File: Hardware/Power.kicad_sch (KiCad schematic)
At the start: 26 parts, among them U2 LT1963AEST-3.3#TRPBF, U3 LT1963AEST-3.3#TRPBF

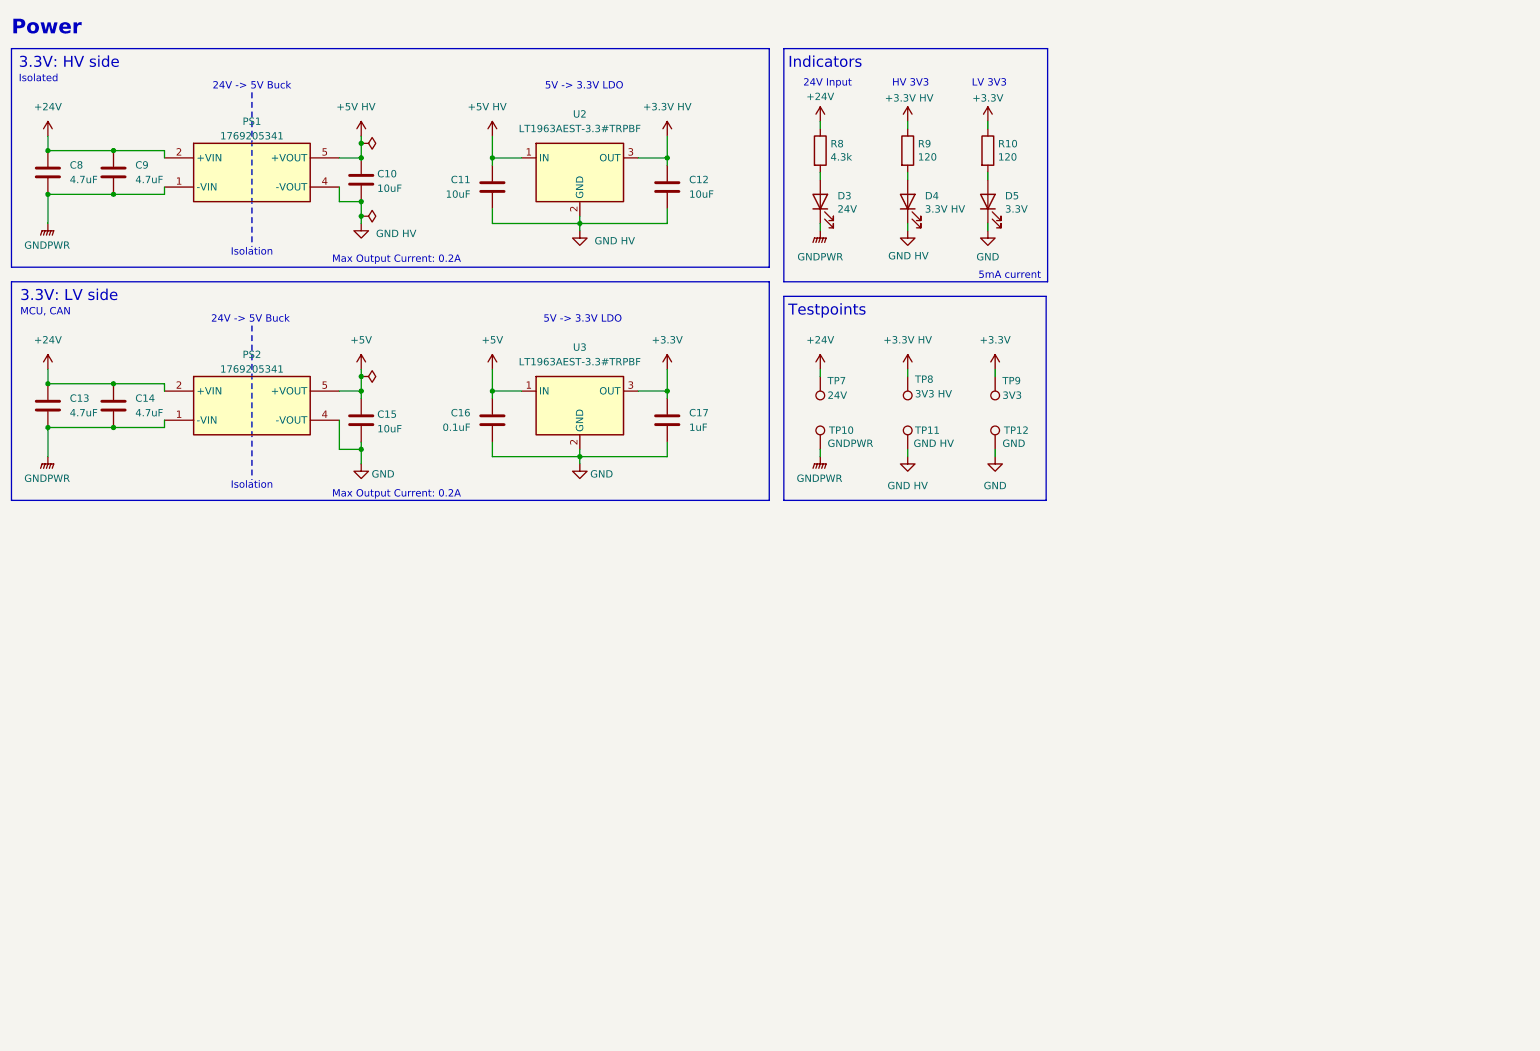
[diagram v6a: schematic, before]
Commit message: 24-5 buck from psom, OR gate for bootload. more sheet organization
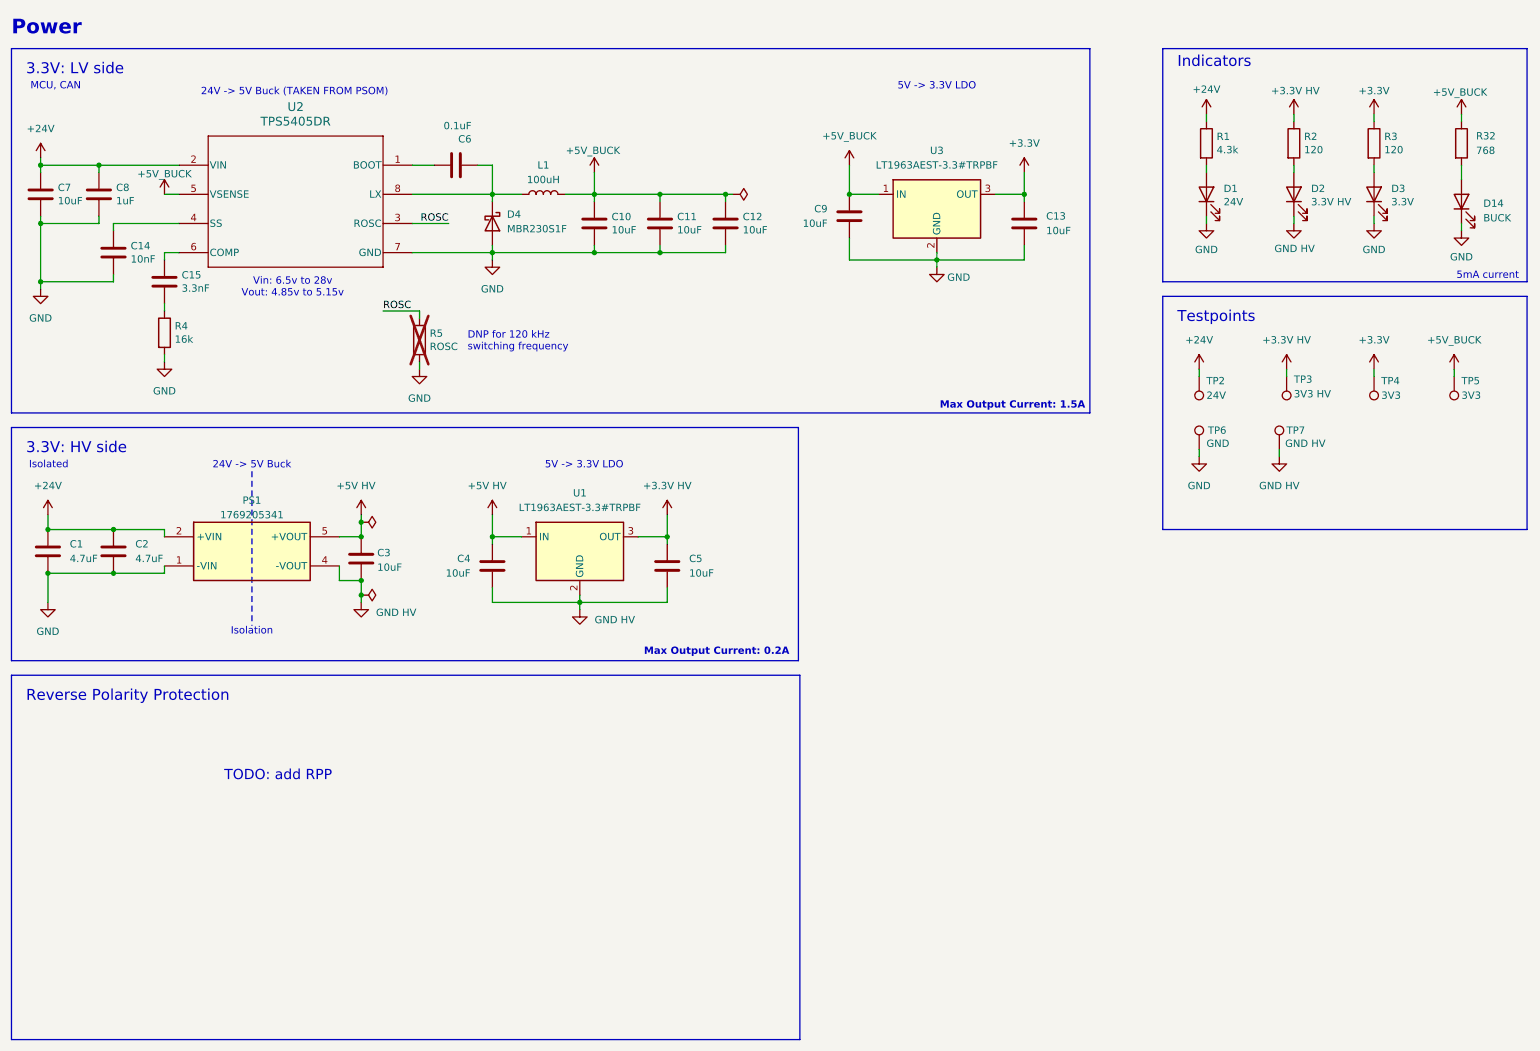
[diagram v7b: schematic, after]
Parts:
- removed C13: 4.7uF, Capacitor_SMD:C_0603_1608Metric_Pad1.08x0.95mm_HandSolder, symbol Device:C
- removed PS2: 1769205341, Parts:WE_1769205341, symbol WE_1769205341:1769205341
- removed TP10: GNDPWR, symbol Connector:TestPoint
- added C10, C11, C12, C7: 10uF, Capacitor_SMD:C_0805_2012Metric_Pad1.18x1.45mm_HandSolder, symbol Device:C
- added C6: 0.1uF, Capacitor_SMD:C_0603_1608Metric_Pad1.08x0.95mm_HandSolder, symbol Device:C
- added C8: 1uF, Capacitor_SMD:C_0603_1608Metric_Pad1.08x0.95mm_HandSolder, symbol Device:C
- added D14: BUCK, LED_SMD:LED_0603_1608Metric_Pad1.05x0.95mm_HandSolder, symbol Device:LED
- added D4: MBR230S1F, Diode_SMD:D_SOD-123F, symbol Device:D_Schottky
- added L1: 100uH, Inductor_SMD:L_Coilcraft_MSS1246-XXX, symbol Device:L
- added R32: 768, Resistor_SMD:R_0603_1608Metric_Pad0.98x0.95mm_HandSolder, symbol Device:R
- added R4: 16k, Resistor_SMD:R_0603_1608Metric_Pad0.98x0.95mm_HandSolder, symbol Device:R
- added R5: ROSC, Resistor_SMD:R_0603_1608Metric_Pad0.98x0.95mm_HandSolder, symbol Device:R
- added TP5: 3V3, symbol Connector:TestPoint
- added U2: TPS5405DR, UTSVT_Power:TPS5405DR, symbol utsvt-power:TPS5405DR
- C13: renamed from C17; value 1uF -> 10uF
- C14: value 4.7uF -> 10nF; P/N (none) -> MSASH168SB5103KTNA01
- C15: value 10uF -> 3.3nF; P/N (none) -> 06035C332K4T2A
- C9: renamed from C16; value 0.1uF -> 10uF
- renumbered C8 to C1, C9 to C2, C10 to C3, C11 to C4, C12 to C5, D3 to D1, D4 to D2, D5 to D3, R8 to R1, R9 to R2, R10 to R3, TP7 to TP2, TP8 to TP3, TP9 to TP4, TP12 to TP6, TP11 to TP7, U2 to U1
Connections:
- net GNDPWR is gone; now on net GND: C1.2, C14.2, C2.2, D1.1 (K), PS1.1 (-VIN)
- net +24V: now also C7.1, C8.1, U2.2 (VIN); no longer C14.1
- net GND: now also C10.2, C11.2, C12.2, C7.2, C8.2, D14.1 (K), D4.2 (A), R4.2, R5.2, U2.7 (GND); no longer C15.2
- net +5V renamed +5V_BUCK
- net +5V_BUCK: now also C10.1, C11.1, C12.1, L1.2, R32.1, TP5.1, U2.5 (VSENSE); no longer C15.1
- new net: C6.2, D4.1 (K), L1.1, U2.8 (LX)
- new net: D14.2 (A), R32.2
- new net: C6.1, U2.1 (BOOT)
- new net: C14.1, U2.4 (SS)
- new net: C15.1, U2.6 (COMP)
- new net: C15.2, R4.1
- new net ROSC: R5.1, U2.3 (ROSC)
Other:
- note added: "24V -> 5V Buck (TAKEN FROM PSOM)"
- note added: "DNP for 120 kHz switching frequency"
- note added: "Max Output Current: 1.5A"
- note added: "Reverse Polarity Protection"
- note added: "TODO: add RPP"
- note added: "Vin: 6.5v to 28v Vout: 4.85v to 5.15v"
- note removed: "24V Input"
- note removed: "HV 3V3"
- note removed: "LV 3V3"
- moved on the sheet: C1, C13, C2, C3, C4, C5, C9, D1, D2, D3, PS1, R1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

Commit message: changed to 2 channel op amp, stole RPP from PSOM
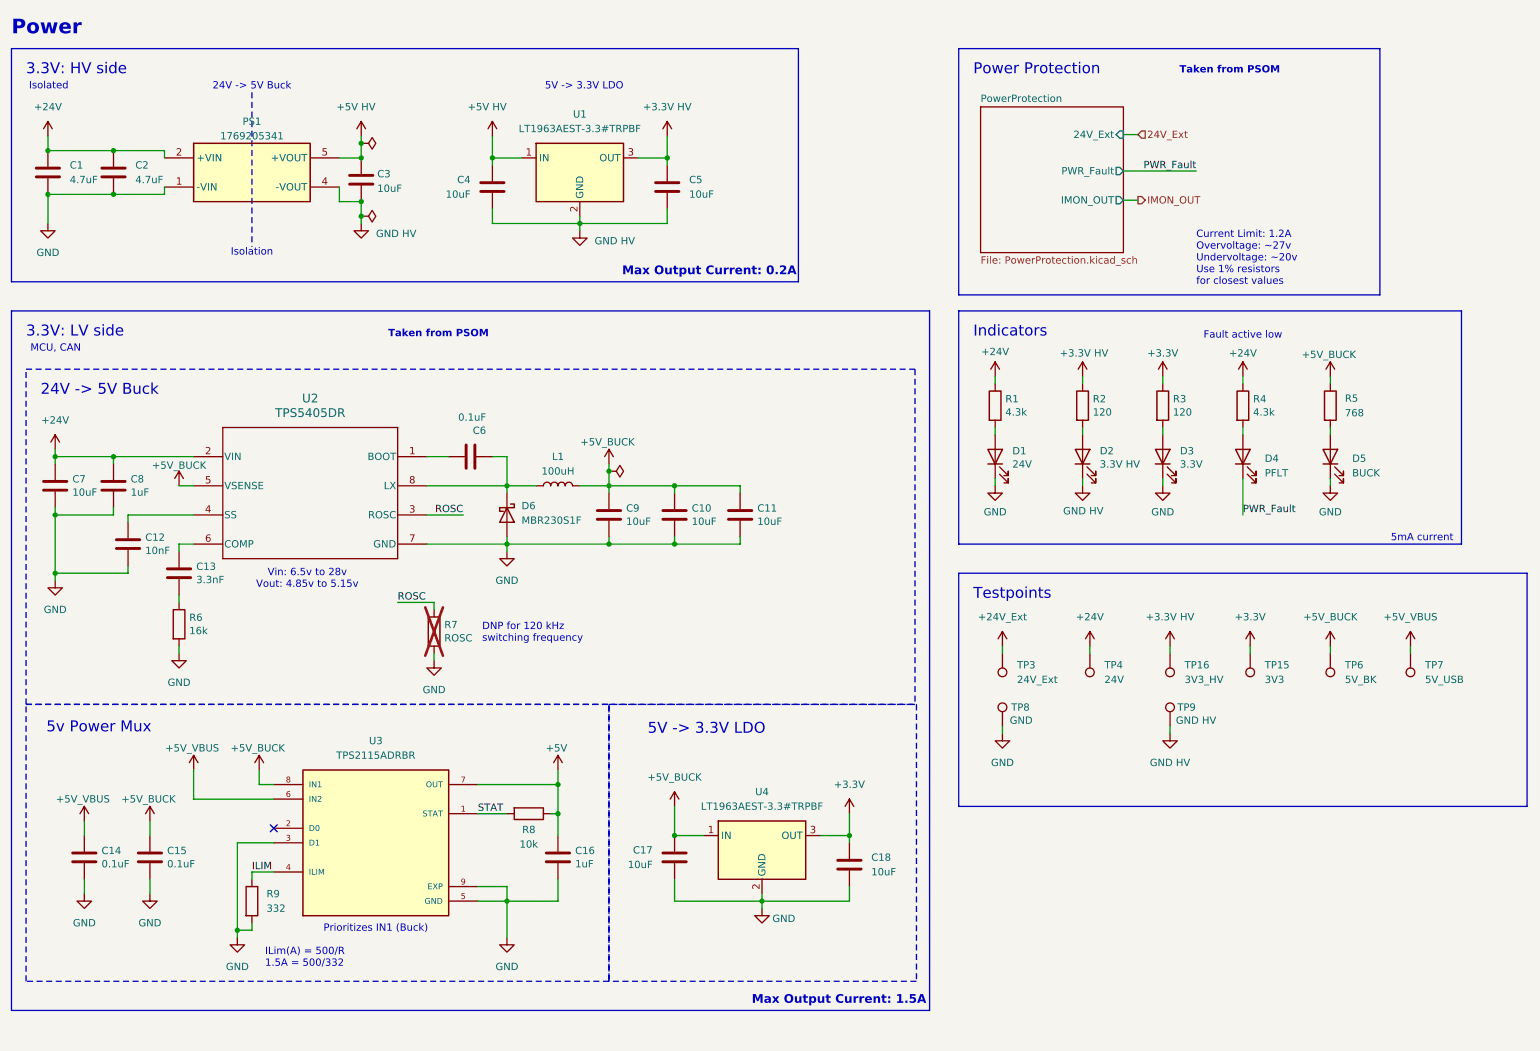
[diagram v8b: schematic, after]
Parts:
- removed TP2: 24V, symbol Connector:TestPoint
- removed TP5: 3V3, symbol Connector:TestPoint
- added C14, C15: 0.1uF, Capacitor_SMD:C_0603_1608Metric_Pad1.08x0.95mm_HandSolder, symbol Device:C
- added C16: 1uF, Capacitor_SMD:C_0603_1608Metric_Pad1.08x0.95mm_HandSolder, symbol Device:C
- added D4: PFLT, LED_SMD:LED_0603_1608Metric_Pad1.05x0.95mm_HandSolder, symbol Device:LED
- added R4: 4.3k, Resistor_SMD:R_0603_1608Metric_Pad0.98x0.95mm_HandSolder, symbol Device:R
- added R8: 10k, Resistor_SMD:R_0603_1608Metric_Pad0.98x0.95mm_HandSolder, symbol Device:R
- added R9: 332, Resistor_SMD:R_0603_1608Metric_Pad0.98x0.95mm_HandSolder, symbol Device:R
- added TP15: 3V3, TestPoint:TestPoint_Pad_1.0x1.0mm, symbol Connector:TestPoint
- added TP16: 3V3_HV, TestPoint:TestPoint_Pad_1.0x1.0mm, symbol Connector:TestPoint
- added TP6: 5V_BK, TestPoint:TestPoint_Pad_1.0x1.0mm, symbol Connector:TestPoint
- added TP7: 5V_USB, TestPoint:TestPoint_Pad_1.0x1.0mm, symbol Connector:TestPoint
- added U3: TPS2115ADRBR, Package_SON:VSON-8-1EP_3x3mm_P0.65mm_EP1.65x2.4mm, symbol TPS2115ADRBR:TPS2115ADRBR
- TP3: value 3V3 HV -> 24V_Ext; footprint (none) -> TestPoint:TestPoint_Pad_1.0x1.0mm; now left out of the parts list
- TP4: value 3V3 -> 24V; footprint (none) -> TestPoint:TestPoint_Pad_1.0x1.0mm; now left out of the parts list
- renumbered C11 to C10, C12 to C11, C14 to C12, C15 to C13, C9 to C17, C13 to C18, C10 to C9, D14 to D5, D4 to D6, R32 to R5, R4 to R6, R5 to R7, TP6 to TP8, TP7 to TP9, U3 to U4
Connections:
- net +24V: now also TP4.1, R4.1
- net +3.3V: now also TP15.1; no longer TP4.1
- net +3.3V HV: now also TP16.1; no longer TP3.1
- net +5V_BUCK: now also C15.1, TP6.1, U3.8 (IN1)
- net GND: now also C14.2, C15.2, C16.2, R9.2, U3.3 (D1), U3.5 (GND), U3.9 (EXP)
- new net: D4.2 (A), R4.2
- new net +24V_Ext: TP3.1
- new net +5V: C16.1, R8.1, U3.7 (OUT)
- new net +5V_VBUS: C14.1, TP7.1, U3.6 (IN2)
- new net ILIM: R9.1, U3.4 (ILIM)
- new net PWR_Fault: D4.1 (K)
- new net STAT: R8.2, U3.1 (STAT)
- no-connect marks 0 -> 1
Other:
- added sheet PowerProtection (PowerProtection.kicad_sch)
- note added: "5v Power Mux"
- note added: "Current Limit: 1.2A Overvoltage: ~27v Undervoltage: ~20v Use 1% resistors for closest values"
- note added: "Fault active low"
- note added: "ILim(A) = 500/R 1.5A = 500/332"
- note added: "Power Protection"
- note added: "Prioritizes IN1 (Buck)"
- note added: "Taken from PSOM"
- note removed: "24V -> 5V Buck (TAKEN FROM PSOM)"
- note removed: "Reverse Polarity Protection"
- note removed: "TODO: add RPP"
- moved on the sheet: C1, C10, C11, C12, C13, C17, C18, C2, C3, C4, C5, C6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
